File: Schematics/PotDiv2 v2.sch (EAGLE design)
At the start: 79 parts, among them IC1 LM358N, IC2 LM358N, IC3 LM358N, IC4 4053N, J1 TERM-BLK-2P, J10 TERM-BLK-2P, J2 TERM-BLK-2P, J3 TERM-BLK-2P, J4 TERM-BLK-2P, J5 TERM-BLK-2P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

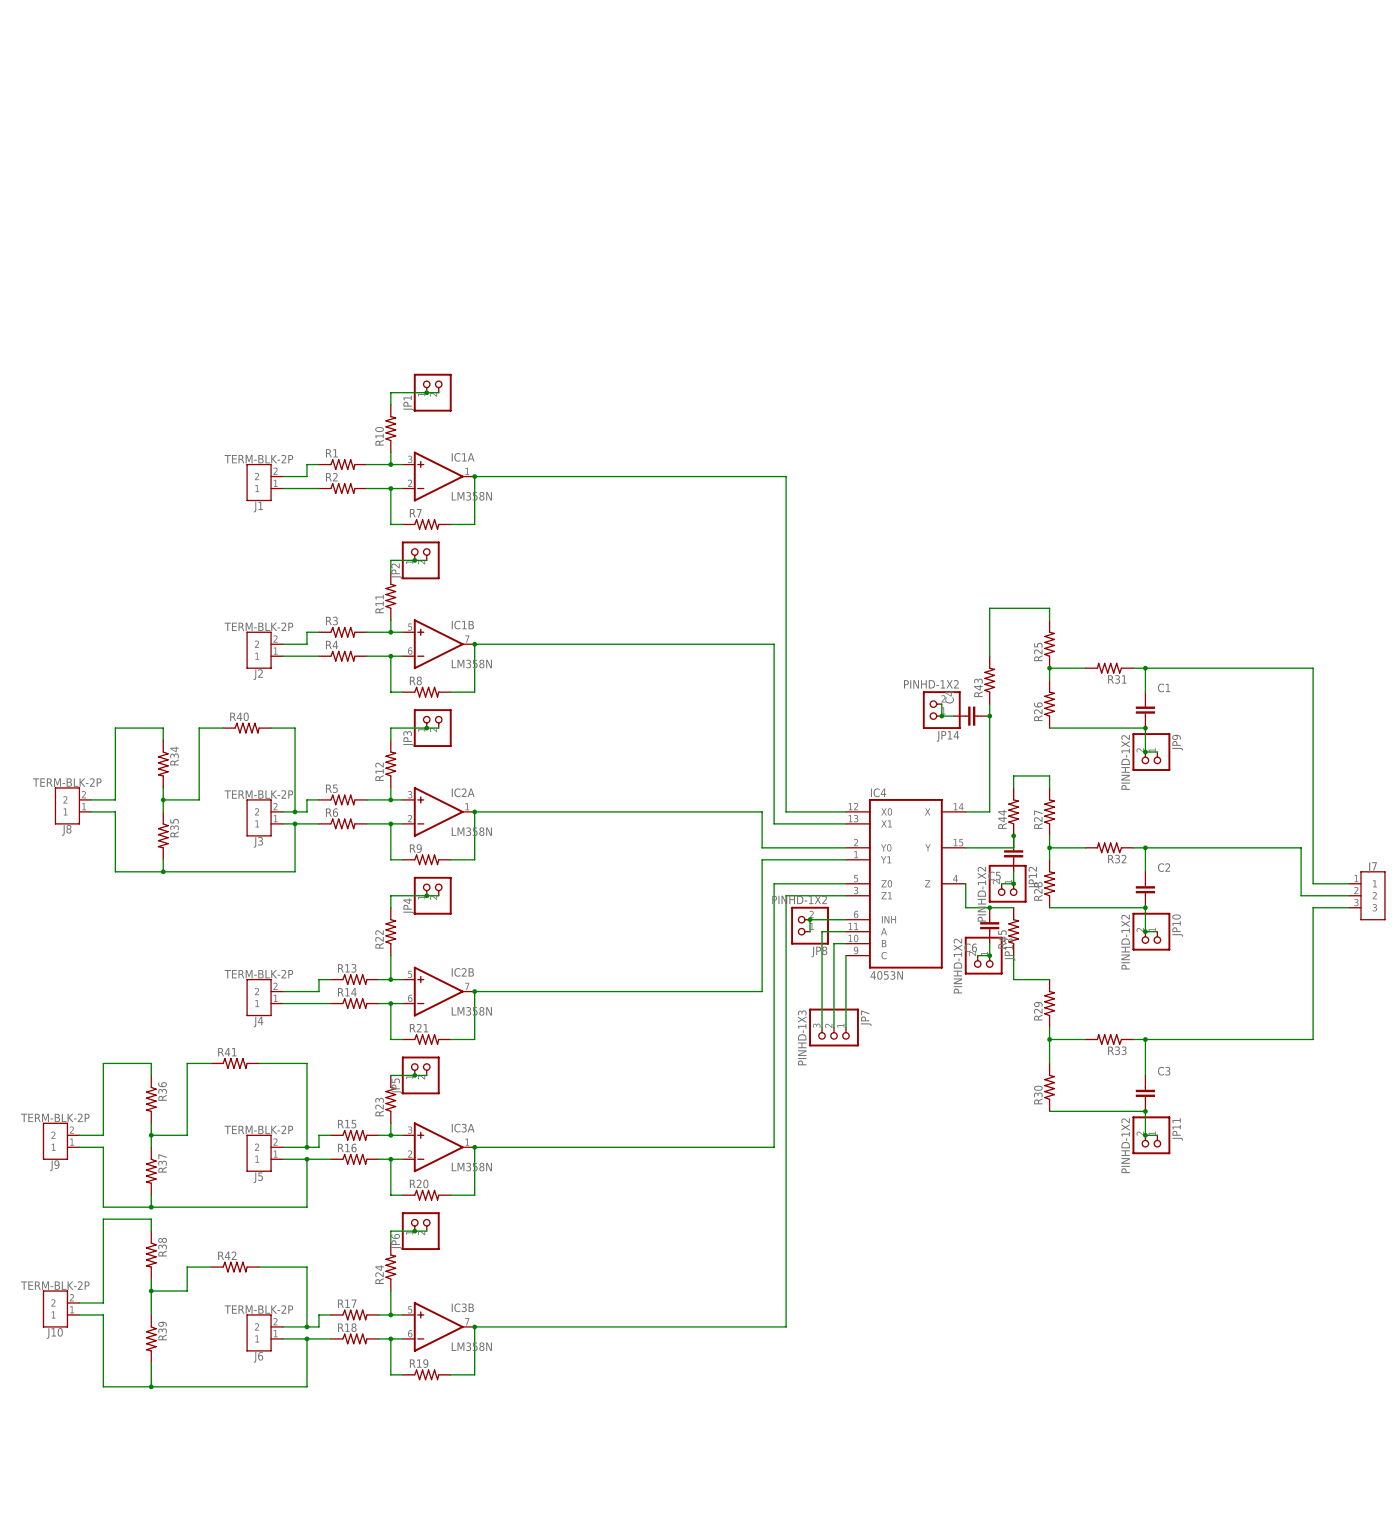
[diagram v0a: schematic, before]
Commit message: CAN & Updated schematics
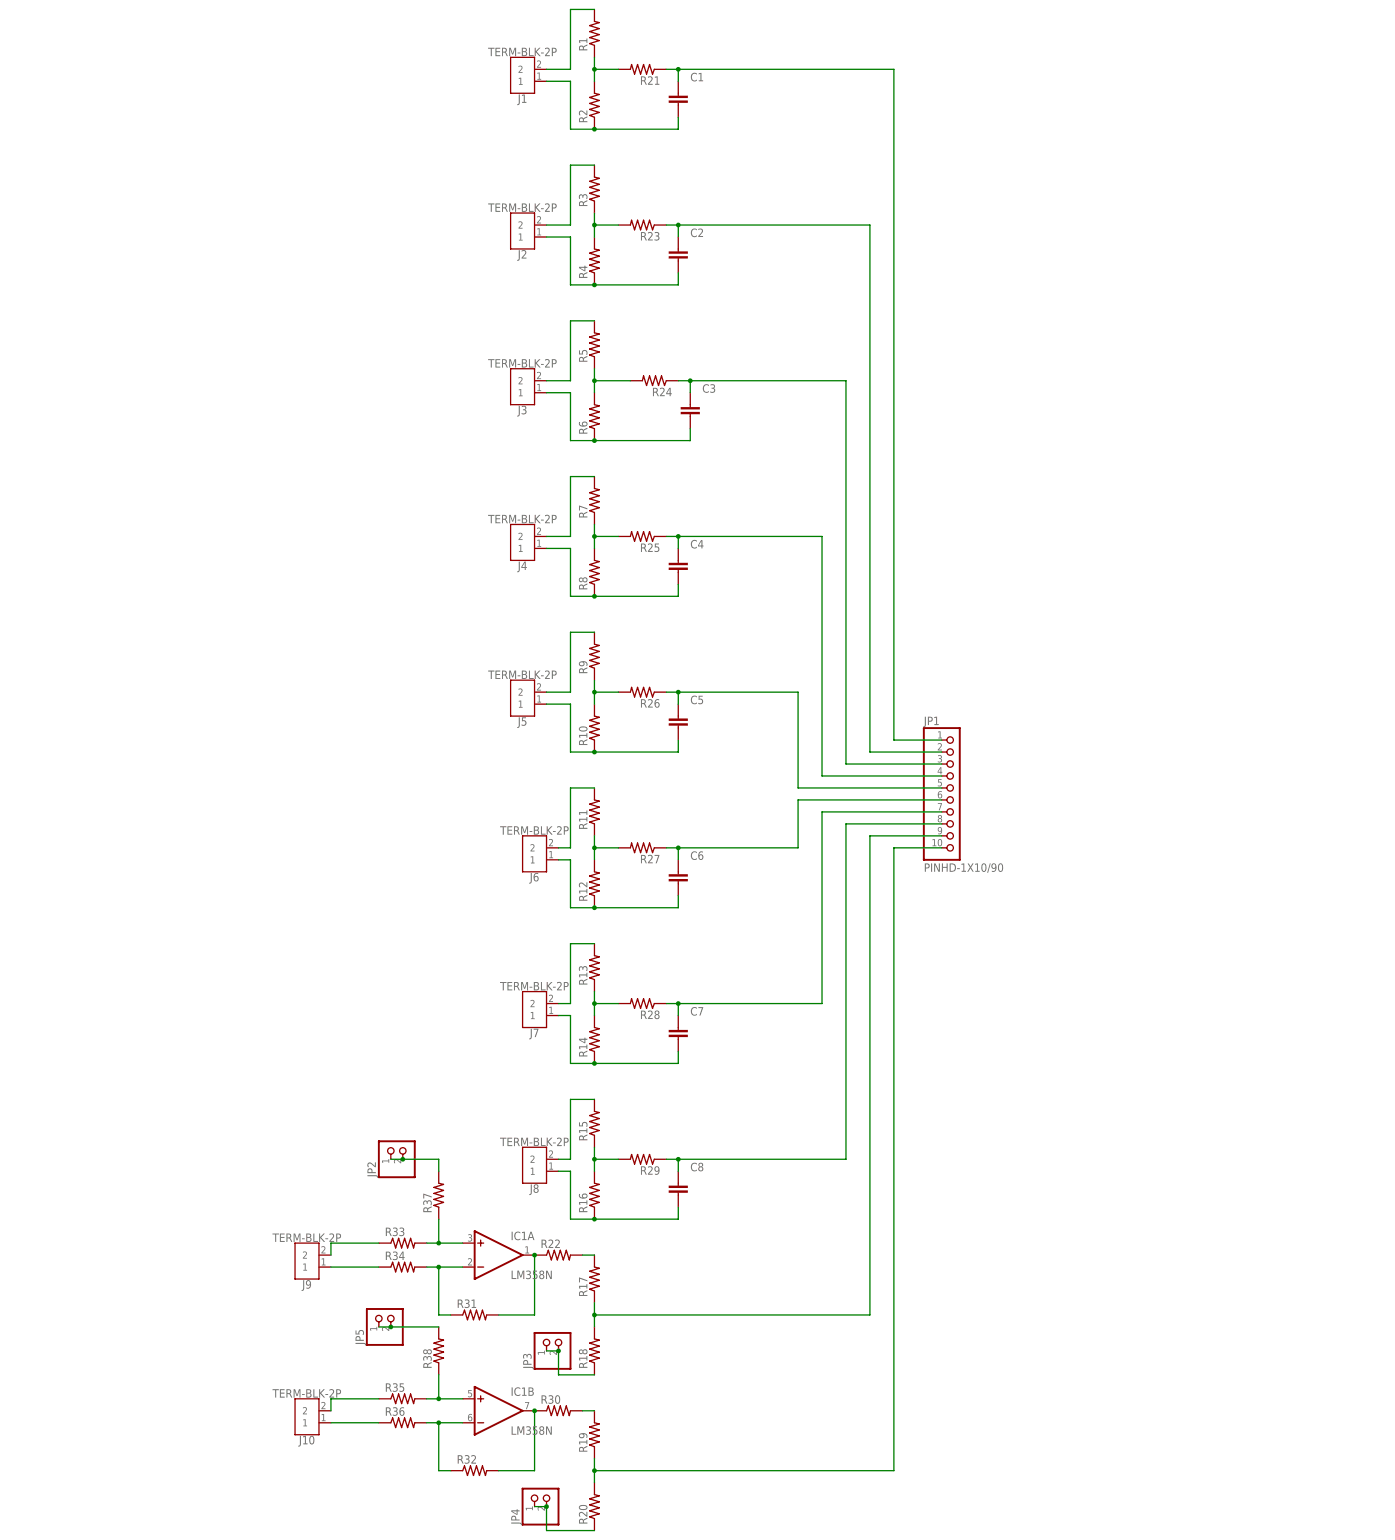
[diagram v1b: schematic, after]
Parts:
- removed IC2, IC3: LM358N, linear:LM358N
- removed IC4: 4053N, 40xx:4053N
- removed JP10, JP11, JP12, JP13, JP14, JP8, JP9: PINHD-1X2, Connector:PINHD-1X2
- removed JP6: (no value), pinhead:PINHD-1X2
- removed JP7: PINHD-1X3, Connector:PINHD-1X3
- removed R39, R40, R41, R42, R43, R44, R45: (no value), Tutorial - Fusion 360:R-US_AXIAL-7.2MM-PITCH
- added C7, C8: (no value), Tutorial - Fusion 360:C_RADIAL-12.5MM-DIA
- J7: value TERM-BLK-3P -> TERM-BLK-2P; device Connector:2828XX-3282837-3 -> Connector:2828XX-2282837-2
- JP1: value (none) -> PINHD-1X10/90; device pinhead:PINHD-1X2 -> Connector:PINHD-1X10/90
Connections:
- removed net N$50: R29.1, R30.2, R33.2
- removed net N$52: C3.1, J7.3, R33.1
- removed net N$53: R25.2, R43.2
- removed net N$54: J8.2, R34.1
- removed net N$55: R34.2, R35.1, R40.1
- removed net N$56: J9.2, R36.1
- removed net N$57: R36.2, R37.1, R41.1
- removed net N$58: C5.2, IC4A.Y, R44.1
- removed net N$59: J10.2, R38.1
- removed net N$60: R29.2, R45.1
- removed net N$61: R38.2, R39.1, R42.1
- removed net N$62: C4.1, JP14.1, JP14.2
- removed net N$63: C5.1, JP12.1, JP12.2
- removed net N$64: C6.1, JP13.1, JP13.2
- net N$1: now also J1.2, R1.2; no longer J1.1, R2.1
- net N$10: now also R24.2, R5.1, R6.2; no longer IC1B.-IN, R4.2, R8.1
- net N$11: now also C3.1, JP1.3, R24.1; no longer JP2.1, JP2.2, R11.2
- net N$12: now also C3.2, J3.1, R6.1; no longer IC1B.OUT, IC4A.X1, R8.2
- net N$13: now also J4.2, R7.2; no longer J3.1, J8.1, R35.2, R6.1
- net N$14: now also R25.2, R7.1, R8.2; no longer J3.2, R40.2, R5.1
- net N$15: now also C4.1, JP1.4, R25.1; no longer IC2A.+IN, R12.1, R5.2
- net N$16: now also C4.2, J4.1, R8.1; no longer JP3.1, JP3.2, R12.2
- net N$17: now also J5.2, R9.2; no longer IC2A.-IN, R6.2, R9.1
- net N$18: now also R10.2, R26.2, R9.1; no longer IC2A.OUT, IC4A.Y0, R9.2
- net N$19: now also C5.2, J5.1, R10.1; no longer J4.1, R14.1
- net N$2: now also R2.2, R21.2; no longer J1.2
- net N$20: now also C5.1, JP1.5, R26.1; no longer J4.2, R13.1
- net N$21: now also J6.2, R11.2; no longer IC2B.+IN, R13.2, R22.1
- net N$22: now also R11.1, R12.2, R27.2; no longer IC2B.-IN, R14.2, R21.1
- net N$23: now also C6.1, JP1.6, R27.1; no longer JP4.1, JP4.2, R22.2
- net N$24: now also C6.2, J6.1, R12.1; no longer IC2B.OUT, IC4A.Y1, R21.2
- net N$25: now also J7.2, R13.2; no longer J5.2, R15.1, R41.2
- net N$26: now also R13.1, R14.2, R28.2; no longer J5.1, J9.1, R16.1, R37.2
- net N$27: now also C7.1, JP1.7, R28.1; no longer IC3A.-IN, R16.2, R20.1
- net N$28: now also C7.2, J7.1, R14.1; no longer IC3A.+IN, R15.2, R23.1
- net N$29: now also J8.2, R15.2; no longer JP5.1, JP5.2, R23.2
- net N$3: now also C1.2, J1.1, R2.1; no longer IC1A.+IN, R1.2, R10.1
- net N$30: now also R15.1, R16.2, R29.2; no longer IC3A.OUT, IC4A.Z0, R20.2
- net N$31: now also C8.1, JP1.8, R29.1; no longer J10.1, J6.1, R18.1, R39.2
- net N$32: now also C8.2, J8.1, R16.1; no longer J6.2, R17.1, R42.2
- net N$33: now also IC1A.OUT, R22.1, R31.2; no longer IC3B.+IN, R17.2, R24.1
- net N$34: now also JP1.9, R17.1, R18.2; no longer JP6.1, JP6.2, R24.2
- net N$35: now also IC1B.+IN, R35.2, R38.1; no longer IC3B.-IN, R18.2, R19.1
- net N$36: now also IC1B.OUT, R30.1, R32.2; no longer IC3B.OUT, IC4A.Z1, R19.2
- net N$37: now also IC1A.+IN, R33.2, R37.1; no longer IC4A.INH, JP8.1, JP8.2
- net N$38: now also JP4.1, JP4.2, R20.1; no longer IC4A.A, JP7.3
- net N$39: now also JP1.10, R19.1, R20.2; no longer IC4A.B, JP7.2
- net N$4: now also C1.1, JP1.1, R21.1; no longer IC1A.-IN, R2.2, R7.1
- net N$40: now also JP2.1, JP2.2, R37.2; no longer IC4A.C, JP7.1
- net N$41: now also IC1A.-IN, R31.1, R34.2; no longer C4.2, IC4A.X, R43.1
- net N$42: now also R17.2, R22.2; no longer R25.1, R26.2, R31.2
- net N$43: now also IC1B.-IN, R32.1, R36.2; no longer C1.2, JP9.1, JP9.2, R26.1
- net N$44: now also R19.2, R30.2; no longer C1.1, J7.1, R31.1
- net N$45: now also J9.2, R33.1; no longer R27.2, R44.2
- net N$46: now also J9.1, R34.1; no longer R27.1, R28.2, R32.2
- net N$47: now also JP5.1, JP5.2, R38.2; no longer C2.1, J7.2, R32.1
- net N$48: now also J10.2, R35.1; no longer C2.2, JP10.1, JP10.2, R28.1
- net N$49: now also J10.1, R36.1; no longer C6.2, IC4A.Z, R45.2
- net N$5: now also J2.2, R3.2; no longer IC1A.OUT, IC4A.X0, R7.2
- net N$51: now also JP3.1, JP3.2, R18.1; no longer C3.2, JP11.1, JP11.2, R30.1
- net N$6: now also R23.2, R3.1, R4.2; no longer JP1.1, JP1.2, R10.2
- net N$7: now also C2.2, J2.1, R4.1; no longer J2.2, R3.1
- net N$8: now also C2.1, JP1.2, R23.1; no longer J2.1, R4.1
- net N$9: now also J3.2, R5.2; no longer IC1B.+IN, R11.1, R3.2
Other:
- moved on the sheet: C1, C2, C3, C4, C5, C6, IC1A, IC1B, J1, J10, J2, J3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
